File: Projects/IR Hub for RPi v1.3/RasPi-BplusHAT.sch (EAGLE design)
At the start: 37 parts, among them SW1 SPST_TACT-KMR2, SW2 SPST_TACT-KMR2, SW3 SPST_TACT-KMR2, T1 2N4401, T2 2N4401, T3 2N4401, T4 2N4401

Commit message: Revert "Revert "relocated IRRCV""
This reverts commit e9af4263ddd1cfc11cb1365f6dffa75911e4cf46.
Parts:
- added U$1, U$2: 74HC2G17-Q100, varshneya:74HC2G17-Q100
- RUN: value (none) -> RST
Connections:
- new net N$12: C2.1, R13.1, SW2.P, SW2.P1, U$1G$2.I
- new net N$13: C3.1, R14.1, R15.1, U$2G$2.I
- new net N$9: C1.1, R12.1, SW1.S, SW1.S1, U$1G$1.I
- net +3V3: now also U$1G$3.VCC, U$2G$3.VCC
- net GND: now also U$1G$3.GND, U$2G$3.GND
- net GPIO17: now also U$1G$1.O; no longer C1.1, R12.1, SW1.S, SW1.S1
- net GPIO27: now also U$1G$2.O; no longer C2.1, R13.1, SW2.P, SW2.P1
- net RST: now also U$2G$2.O; no longer C3.1, R14.1, R15.1
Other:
- moved on the sheet: C1, C2, C3, R12, R13, R14, R15, SW1, SW2, SW3

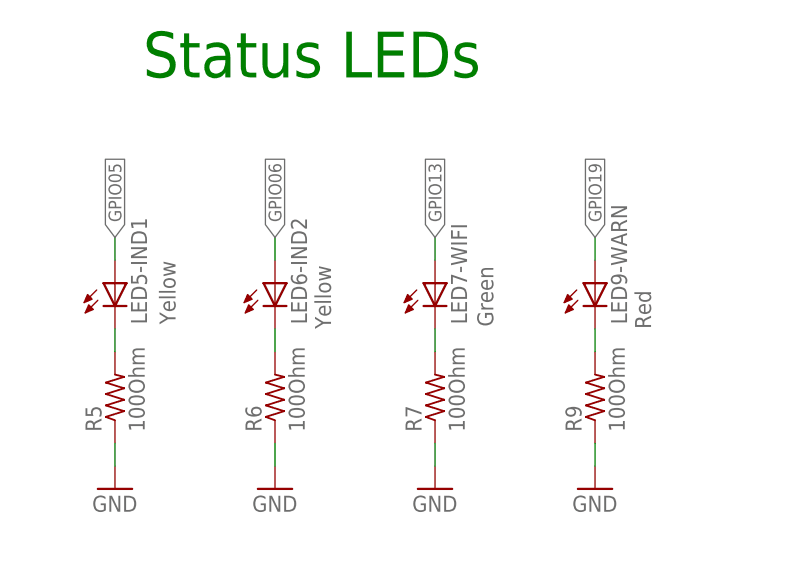
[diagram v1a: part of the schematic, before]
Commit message: minor teaks to silk, changed one LED to blue color
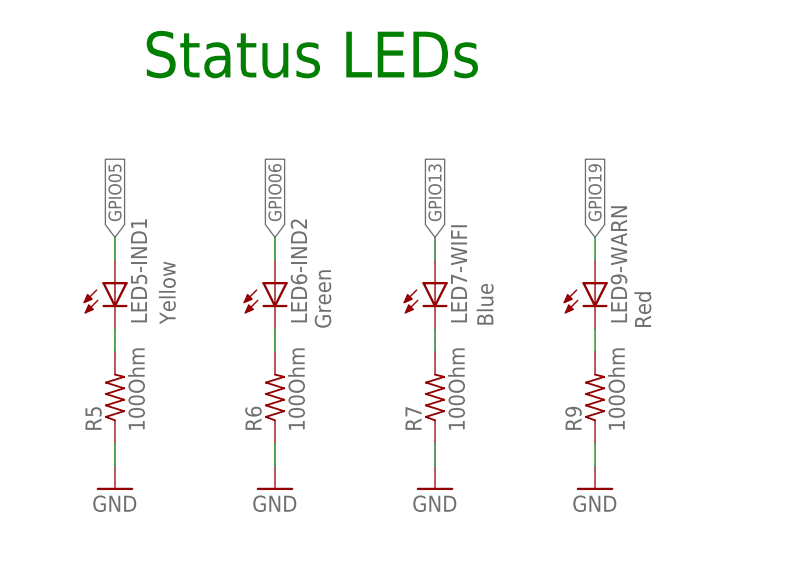
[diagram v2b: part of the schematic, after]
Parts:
- LED6-IND2: value Yellow -> Green; MPN 150080YS75000 -> 150080GS75000; OC_NEWARK 95W3804 -> 95W3800
- LED7-WIFI: value Green -> Blue; MPN 150080GS75000 -> 150080BS75000; OC_NEWARK 95W3800 -> 95W3799
- R14: MPN CRCW080510K0FKEA -> CRCW08051M00FKEA; OC_NEWARK 52K9795 -> 52K9759
- R15: MPN CRCW080510K0FKEA -> CRCW0805100KFKEA; OC_NEWARK 52K9795 -> 52K9808
- U$1, U$2: MPN (none) -> 74HC2G17GW,125; OC_NEWARK (none) -> 71R2196
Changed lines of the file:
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@@
 </part>
 <part name="GND4" library="supply1" deviceset="GND" device=""/>
-<part name="LED6-IND2" library="led" deviceset="LED" device="CHIPLED_0805" value="Yellow">
-<attribute name="MF" value=""/>
-<attribute name="MPN" value="150080YS75000"/>
-<attribute name="OC_NEWARK" value="95W3804"/>
+<part name="LED6-IND2" library="led" deviceset="LED" device="CHIPLED_0805" value="Green">
+<attribute name="MF" value=""/>
+<attribute name="MPN" value="150080GS75000"/>
+<attribute name="OC_NEWARK" value="95W3800"/>
 </part>
 <part name="R6" library="adafruit" deviceset="R-US_" device="R0805" value="100Ohm">
@@
 </part>
 <part name="GND8" library="supply1" deviceset="GND" device=""/>
-<part name="LED7-WIFI" library="led" deviceset="LED" device="CHIPLED_0805" value="Green">
-<attribute name="MF" value=""/>
-<attribute name="MPN" value="150080GS75000"/>
-<attribute name="OC_NEWARK" value="95W3800"/>
+<part name="LED7-WIFI" library="led" deviceset="LED" device="CHIPLED_0805" value="Blue">
+<attribute name="MF" value=""/>
+<attribute name="MPN" value="150080BS75000"/>
+<attribute name="OC_NEWARK" value="95W3799"/>
 </part>
 <part name="R7" library="adafruit" deviceset="R-US_" device="R0805" value="100Ohm">
@@
 <part name="R14" library="adafruit" deviceset="R-US_" device="R0805" value="1M">
 <attribute name="MF" value="VISHAY/DALE"/>
-<attribute name="MPN" value="CRCW080510K0FKEA"/>
-<attribute name="OC_NEWARK" value="52K9795"/>
+<attribute name="MPN" value="CRCW08051M00FKEA"/>
+<attribute name="OC_NEWARK" value="52K9759"/>
 </part>
 <part name="C3" library="adafruit" deviceset="C-US" device="C0805" value="1uF">
@@
 <part name="R15" library="adafruit" deviceset="R-US_" device="R0805" value="100K">
 <attribute name="MF" value="VISHAY/DALE"/>
-<attribute name="MPN" value="CRCW080510K0FKEA"/>
-<attribute name="OC_NEWARK" value="52K9795"/>
-</part>
-<part name="U$1" library="varshneya" deviceset="74HC2G17-Q100" device=""/>
-<part name="U$2" library="varshneya" deviceset="74HC2G17-Q100" device=""/>
+<attribute name="MPN" value="CRCW0805100KFKEA"/>
+<attribute name="OC_NEWARK" value="52K9808"/>
+</part>
+<part name="U$1" library="varshneya" deviceset="74HC2G17-Q100" device="">
+<attribute name="MF" value=""/>
+<attribute name="MPN" value="74HC2G17GW,125"/>
+<attribute name="OC_NEWARK" value="71R2196"/>
+</part>
+<part name="U$2" library="varshneya" deviceset="74HC2G17-Q100" device="">
+<attribute name="MF" value=""/>
+<attribute name="MPN" value="74HC2G17GW,125"/>
+<attribute name="OC_NEWARK" value="71R2196"/>
+</part>
 <part name="+3V4" library="supply1" deviceset="+3V3" device=""/>
 <part name="GND13" library="supply1" deviceset="GND" device=""/>
@@
 <attribute name="NAME" x="279.4" y="201.295" size="1.778" layer="95"/>
 <attribute name="VALUE" x="279.4" y="193.04" size="1.778" layer="96"/>
+<attribute name="OC_NEWARK" x="284.48" y="198.12" size="1.4224" layer="96" display="off"/>
+<attribute name="MF" x="284.48" y="198.12" size="1.4224" layer="96" display="off"/>
+<attribute name="MPN" x="284.48" y="198.12" size="1.4224" layer="96" display="off"/>
 </instance>
 <instance part="U$1" gate="G$2" x="345.44" y="198.12" smashed="yes">
@@
 </instance>
 <instance part="U$1" gate="G$3" x="243.84" y="195.58"/>
-<instance part="U$2" gate="G$1" x="347.98" y="132.08"/>
+<instance part="U$2" gate="G$1" x="347.98" y="132.08">
+<attribute name="OC_NEWARK" x="347.98" y="132.08" size="1.4224" layer="96" display="off"/>
+<attribute name="MF" x="347.98" y="132.08" size="1.4224" layer="96" display="off"/>
+<attribute name="MPN" x="347.98" y="132.08" size="1.4224" layer="96" display="off"/>
+</instance>
 <instance part="U$2" gate="G$2" x="292.1" y="127"/>
 <instance part="U$2" gate="G$3" x="327.66" y="129.54"/>

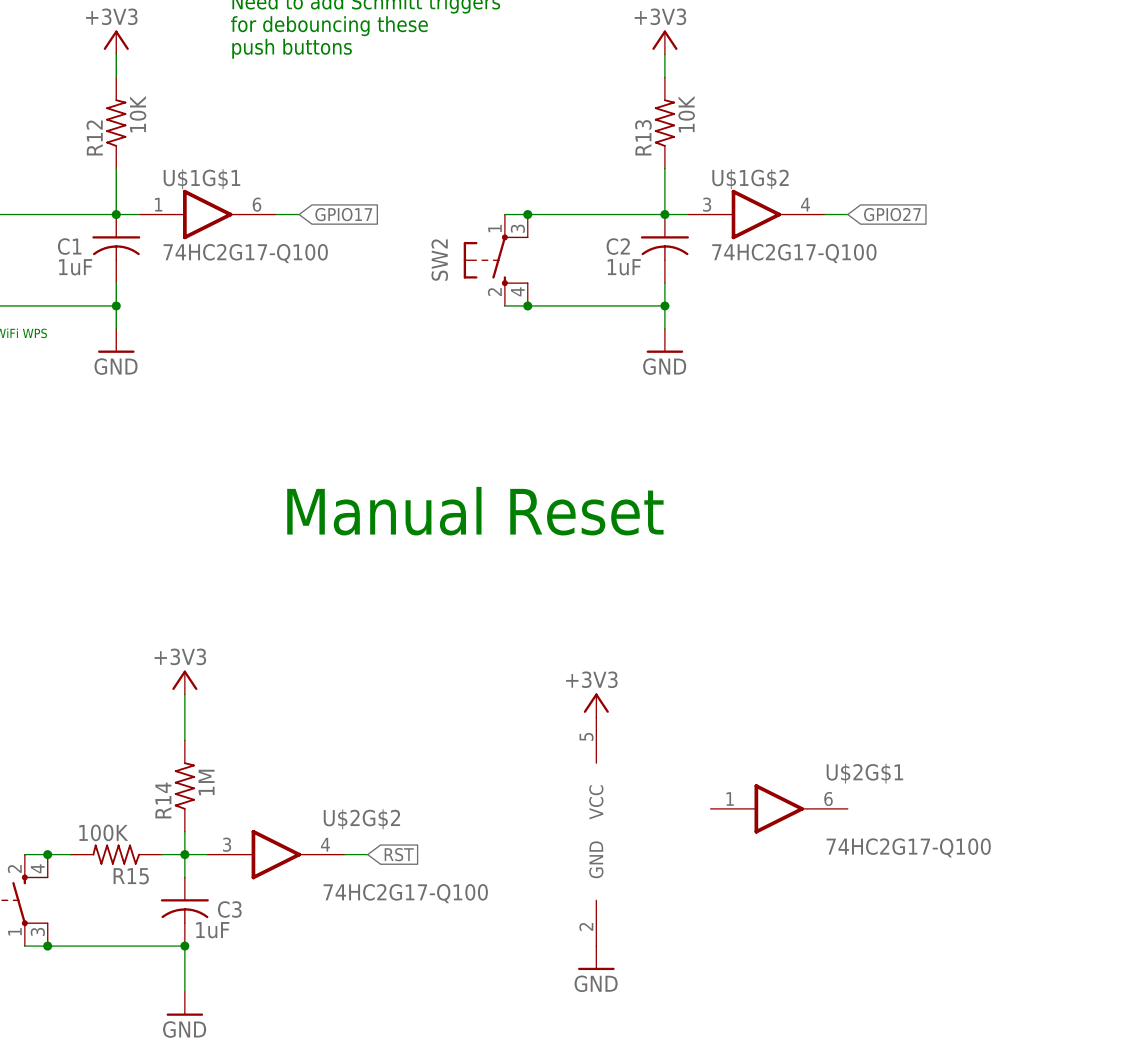
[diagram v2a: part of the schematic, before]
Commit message: near final version - checkpoint
Pending AIs -
check polarity of the IR LEDs
check the buffer circuit on breadboard
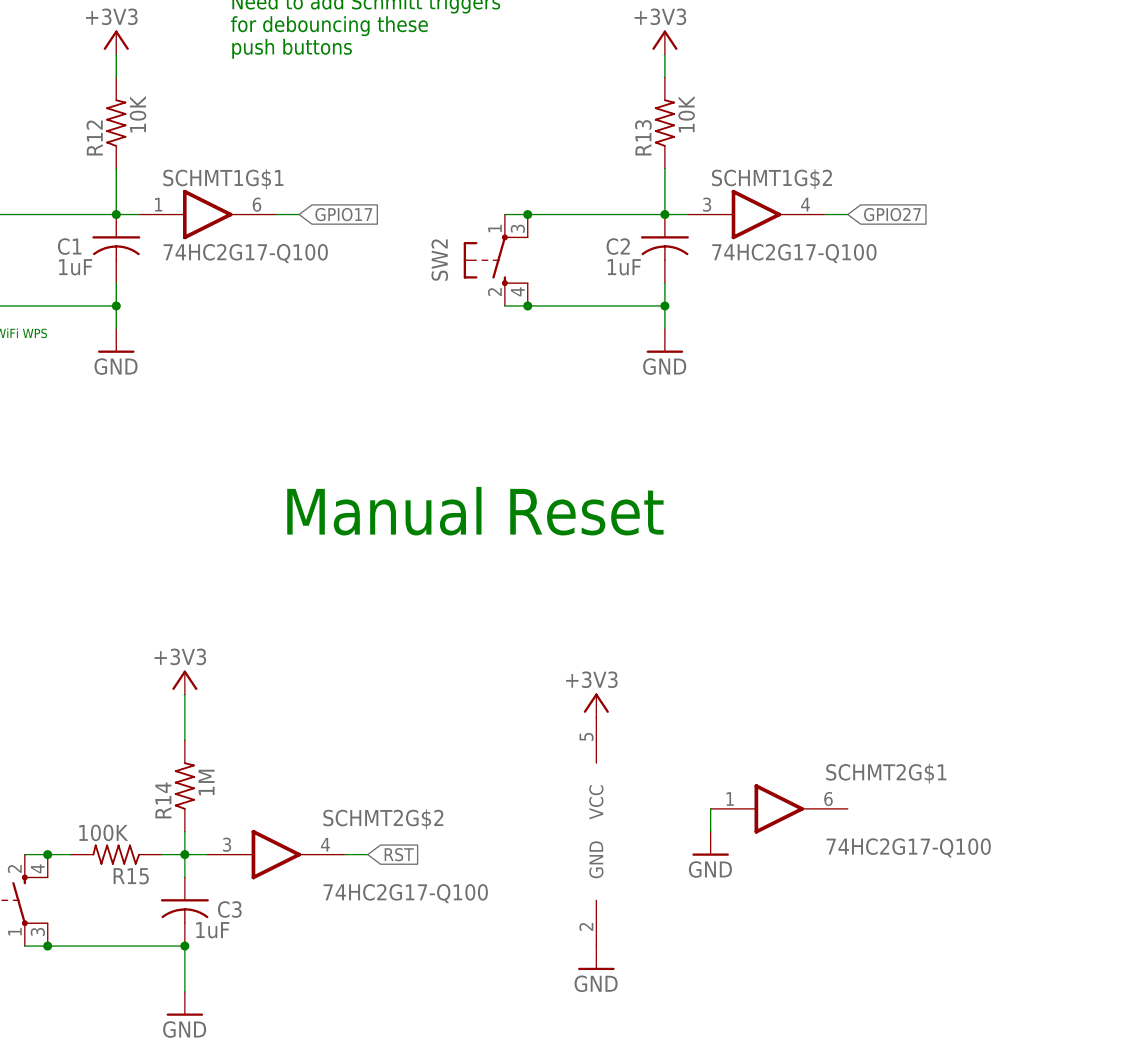
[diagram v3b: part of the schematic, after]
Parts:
- renumbered U$1 to SCHMT1, U$2 to SCHMT2
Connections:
- net GND: now also SCHMT2G$1.I
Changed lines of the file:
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@@
 <attribute name="OC_NEWARK" value="52K9808"/>
 </part>
-<part name="U$1" library="varshneya" deviceset="74HC2G17-Q100" device="">
+<part name="SCHMT1" library="varshneya" deviceset="74HC2G17-Q100" device="">
 <attribute name="MF" value=""/>
 <attribute name="MPN" value="74HC2G17GW,125"/>
 <attribute name="OC_NEWARK" value="71R2196"/>
 </part>
-<part name="U$2" library="varshneya" deviceset="74HC2G17-Q100" device="">
+<part name="SCHMT2" library="varshneya" deviceset="74HC2G17-Q100" device="">
 <attribute name="MF" value=""/>
 <attribute name="MPN" value="74HC2G17GW,125"/>
@@
 <part name="GND14" library="supply1" deviceset="GND" device=""/>
 <part name="+3V5" library="supply1" deviceset="+3V3" device=""/>
+<part name="GND16" library="supply1" deviceset="GND" device=""/>
 </parts>
 <sheets>
@@
 <attribute name="VALUE" x="275.59" y="130.302" size="1.778" layer="96" rot="R180"/>
 </instance>
-<instance part="U$1" gate="G$1" x="284.48" y="198.12" smashed="yes">
+<instance part="SCHMT1" gate="G$1" x="284.48" y="198.12" smashed="yes">
 <attribute name="NAME" x="279.4" y="201.295" size="1.778" layer="95"/>
 <attribute name="VALUE" x="279.4" y="193.04" size="1.778" layer="96"/>
@@
 <attribute name="MPN" x="284.48" y="198.12" size="1.4224" layer="96" display="off"/>
 </instance>
-<instance part="U$1" gate="G$2" x="345.44" y="198.12" smashed="yes">
+<instance part="SCHMT1" gate="G$2" x="345.44" y="198.12" smashed="yes">
 <attribute name="NAME" x="340.36" y="201.295" size="1.778" layer="95"/>
 <attribute name="VALUE" x="340.36" y="193.04" size="1.778" layer="96"/>
 </instance>
-<instance part="U$1" gate="G$3" x="243.84" y="195.58"/>
-<instance part="U$2" gate="G$1" x="347.98" y="132.08">
+<instance part="SCHMT1" gate="G$3" x="243.84" y="195.58"/>
+<instance part="SCHMT2" gate="G$1" x="347.98" y="132.08">
 <attribute name="OC_NEWARK" x="347.98" y="132.08" size="1.4224" layer="96" display="off"/>
 <attribute name="MF" x="347.98" y="132.08" size="1.4224" layer="96" display="off"/>
 <attribute name="MPN" x="347.98" y="132.08" size="1.4224" layer="96" display="off"/>
 </instance>
-<instance part="U$2" gate="G$2" x="292.1" y="127"/>
-<instance part="U$2" gate="G$3" x="327.66" y="129.54"/>
+<instance part="SCHMT2" gate="G$2" x="292.1" y="127"/>
+<instance part="SCHMT2" gate="G$3" x="327.66" y="129.54"/>
 <instance part="+3V4" gate="G$1" x="243.84" y="213.36" smashed="yes">
 <attribute name="VALUE" x="246.38" y="215.9" size="1.778" layer="96" rot="R180"/>
@@
 <attribute name="VALUE" x="330.2" y="147.32" size="1.778" layer="96" rot="R180"/>
 </instance>
+<instance part="GND16" gate="1" x="340.36" y="127"/>
 </instances>
 <busses>
@@
 </segment>
 <segment>
-<pinref part="U$1" gate="G$3" pin="GND"/>
+<pinref part="SCHMT1" gate="G$3" pin="GND"/>
 <pinref part="GND13" gate="1" pin="GND"/>
 <wire x1="243.84" y1="180.34" x2="243.84" y2="182.88" width="0.1524" layer="91"/>
 </segment>
 <segment>
-<pinref part="U$2" gate="G$3" pin="GND"/>
+<pinref part="SCHMT2" gate="G$3" pin="GND"/>
 <pinref part="GND14" gate="1" pin="GND"/>
+</segment>
+<segment>
+<pinref part="SCHMT2" gate="G$1" pin="I"/>
+<pinref part="GND16" gate="1" pin="GND"/>
+<wire x1="340.36" y1="129.54" x2="340.36" y2="132.08" width="0.1524" layer="91"/>
 </segment>
 </net>
@@
 </segment>
 <segment>
-<pinref part="U$1" gate="G$3" pin="VCC"/>
+<pinref part="SCHMT1" gate="G$3" pin="VCC"/>
 <pinref part="+3V4" gate="G$1" pin="+3V3"/>
 <wire x1="243.84" y1="210.82" x2="243.84" y2="208.28" width="0.1524" layer="91"/>
 </segment>
 <segment>
-<pinref part="U$2" gate="G$3" pin="VCC"/>
+<pinref part="SCHMT2" gate="G$3" pin="VCC"/>
 <pinref part="+3V5" gate="G$1" pin="+3V3"/>
 </segment>
@@
 <wire x1="292.1" y1="198.12" x2="294.64" y2="198.12" width="0.1524" layer="91"/>
 <label x="294.64" y="198.12" size="1.4224" layer="95" xref="yes"/>
-<pinref part="U$1" gate="G$1" pin="O"/>
+<pinref part="SCHMT1" gate="G$1" pin="O"/>
 </segment>
 </net>
@@
 <wire x1="353.06" y1="198.12" x2="355.6" y2="198.12" width="0.1524" layer="91"/>
 <label x="355.6" y="198.12" size="1.4224" layer="95" xref="yes"/>
-<pinref part="U$1" gate="G$2" pin="O"/>
+<pinref part="SCHMT1" gate="G$2" pin="O"/>
 </segment>
 </net>
@@
 </segment>
 <segment>
-<pinref part="U$2" gate="G$2" pin="O"/>
+<pinref part="SCHMT2" gate="G$2" pin="O"/>
 <wire x1="299.72" y1="127" x2="302.26" y2="127" width="0.1524" layer="91"/>
 <label x="302.26" y="127" size="1.4224" layer="95" xref="yes"/>
@@
 <junction x="274.32" y="198.12"/>
 <wire x1="276.86" y1="198.12" x2="274.32" y2="198.12" width="0.1524" layer="91"/>
-<pinref part="U$1" gate="G$1" pin="I"/>
+<pinref part="SCHMT1" gate="G$1" pin="I"/>
 </segment>
 </net>
@@
 <junction x="335.28" y="198.12"/>
 <wire x1="337.82" y1="198.12" x2="335.28" y2="198.12" width="0.1524" layer="91"/>
-<pinref part="U$1" gate="G$2" pin="I"/>
+<pinref part="SCHMT1" gate="G$2" pin="I"/>
 </segment>
 </net>
@@
 <segment>
 <pinref part="R15" gate="G$1" pin="1"/>
-<pinref part="U$2" gate="G$2" pin="I"/>
+<pinref part="SCHMT2" gate="G$2" pin="I"/>
 <wire x1="279.4" y1="127" x2="281.94" y2="127" width="0.1524" layer="91"/>
 <pinref part="R14" gate="G$1" pin="1"/>
